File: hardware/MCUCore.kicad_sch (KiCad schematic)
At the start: 1 part, among them U1 ESP32-WROOM-32E

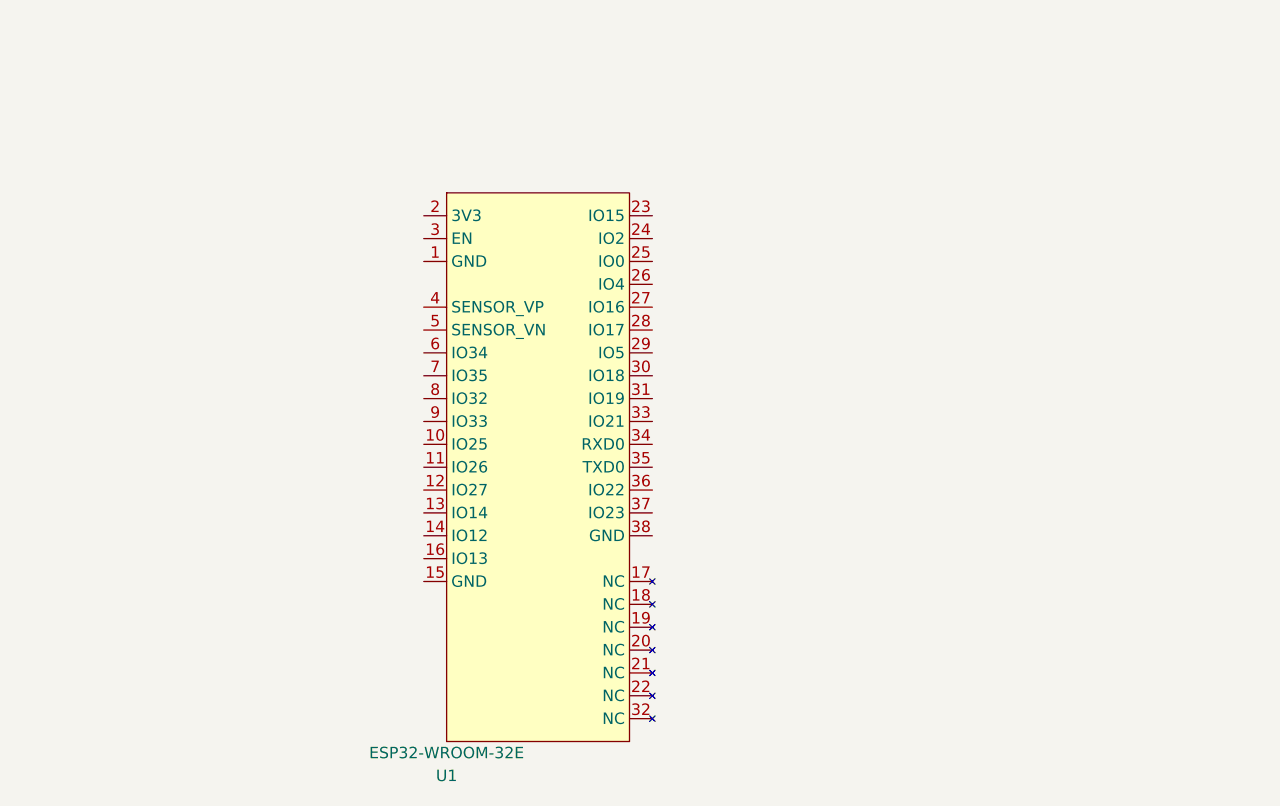
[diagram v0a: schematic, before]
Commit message: Populate MCU Core sheet
ESP32-WROOM-32E (U1) fully wired:
- Decoupling (C1 100nF + C2 1uF on 3V3/GND)
- EN: 10k pull-up + 100nF delay cap + manual RESET button
- BOOT (IO0): 10k pull-up + manual BOOT button
- nFAULT (IO15): 10k pull-up (also the MTDO safe-boot-strap default)
- UART0 header (J1, 1x4: 3V3/TX0/RX0/GND) - doubles as flashing +
  control/telemetry interface
- Expansion header (J2, 1x4: EXP1-3 on IO25/26/27 + GND) for optional
  hall/encoder sensors
- All cross-sheet signals (SPI to gate driver, SOA/SOB/SOC current
  sense, CAN TX/RX, DC-bus + temperature sense) as global labels per
  the pin map in ARCHITECTURE.md
- All 12 unused/NC pins flagged no_connect
- ERC clean except expected cross-sheet-driver warnings (will resolve
  once Power Supply/Gate Drive/Communication/Current Sensing sheets
  are wired) and a known cosmetic text-variable-resolution quirk in
  this MCP session (verified correct on disk, resolves on reopen in
  KiCad UI)

Co-Authored-By: Claude Sonnet 5 <noreply@anthropic.com>
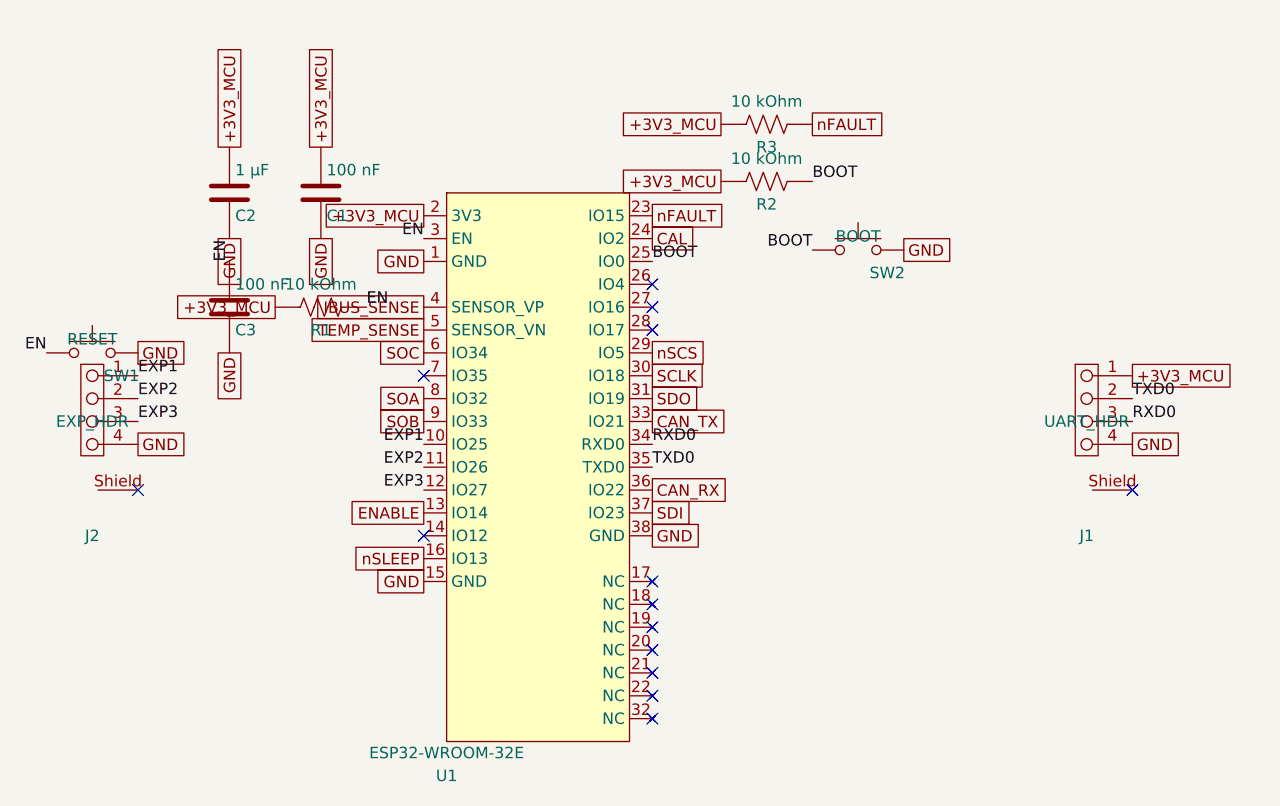
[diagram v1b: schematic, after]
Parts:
- added C1, C3: 100 nF, symbol METUPowerLab_Capacitors_Ceramics_SurfaceMounts:100 nF
- added C2: 1 µF, symbol METUPowerLab_Capacitors_Ceramics_SurfaceMounts:1 µF
- added J1: UART_HDR, METUPowerLab_Connectors_SignalConnectors:2147210040, symbol METUPowerLab_Connectors_SignalConnectors:2147210040
- added J2: EXP_HDR, METUPowerLab_Connectors_SignalConnectors:384471-E, symbol METUPowerLab_Connectors_SignalConnectors:384471-E
- added R1, R2, R3: 10 kOhm, symbol METUPowerLab_Resistors_ChipResistors:10 kOhm
- added SW1: RESET, METUPowerLab_Switches_TactileSwitches:TL6330AF200Q, symbol METUPowerLab_Switches_TactileSwitches:TL6330AF200Q
- added SW2: BOOT, METUPowerLab_Switches_TactileSwitches:TL6330AF200Q, symbol METUPowerLab_Switches_TactileSwitches:TL6330AF200Q
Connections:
- net GND: now reaches U1.1 (GND)
- net GND: now also U1.15 (GND), U1.38 (GND), C1.2, C2.2, C3.2, J1.4, J2.4, SW1.2, SW2.2
- net EXP1: now reaches U1.10 (IO25)
- net EXP1: now also J2.1
- net EXP2: now reaches U1.11 (IO26)
- net EXP2: now also J2.2
- net EXP3: now reaches U1.12 (IO27)
- net EXP3: now also J2.3
- net ENABLE: now reaches U1.13 (IO14)
- net nSLEEP: now reaches U1.16 (IO13)
- net +3V3_MCU: now reaches U1.2 (3V3)
- net +3V3_MCU: now also C1.1, C2.1, J1.1, R1.1, R2.1, R3.1
- net nFAULT: now reaches U1.23 (IO15)
- net nFAULT: now also R3.2
- net CAL: now reaches U1.24 (IO2)
- net BOOT: now reaches U1.25 (IO0)
- net BOOT: now also R2.2, SW2.1
- net nSCS: now reaches U1.29 (IO5)
- net EN: now reaches U1.3 (EN)
- net EN: now also C3.1, R1.2, SW1.1
- net SCLK: now reaches U1.30 (IO18)
- net SDO: now reaches U1.31 (IO19)
- net CAN_TX: now reaches U1.33 (IO21)
- net RXD0: now reaches U1.34 (RXD0)
- net RXD0: now also J1.3
- net TXD0: now reaches U1.35 (TXD0)
- net TXD0: now also J1.2
- net CAN_RX: now reaches U1.36 (IO22)
- net SDI: now reaches U1.37 (IO23)
- net IBUS_SENSE: now reaches U1.4 (SENSOR_VP)
- net TEMP_SENSE: now reaches U1.5 (SENSOR_VN)
- net SOC: now reaches U1.6 (IO34)
- net SOA: now reaches U1.8 (IO32)
- net SOB: now reaches U1.9 (IO33)
- no-connect marks 0 -> 14

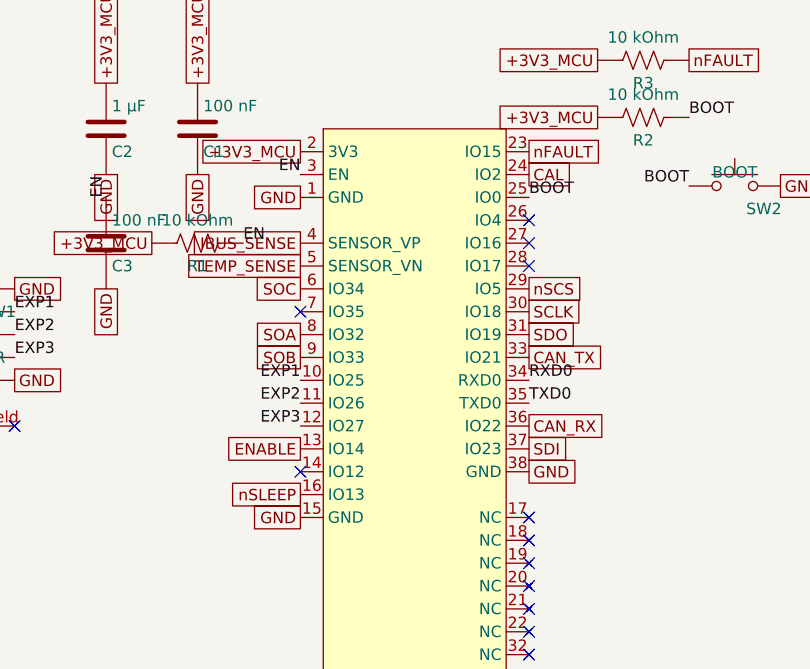
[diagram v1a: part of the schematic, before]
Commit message: Populate Gate Drive sheet (DRV8323R), fix MCU Core PWM pin gap
- DRV8323RSRGZT (=DRV8323R) fully wired per the real TI datasheet
  (SLVSDJ3D, fetched directly): single shared charge pump (not
  per-phase bootstrap caps as originally assumed), VDD/DVDD internal
  LDO decoupling only, VREF self-referenced, optional 600mA buck
  disabled (nSHD tied to GND), CAL tied to GND
- Caught and fixed a real gap before it became a wiring mistake: the
  chip needs 6 direct hardware PWM pins (INHA/INLA/INHB/INLB/INHC/
  INLC) in addition to SPI - missed in the first pass. Also removed a
  fictitious 'nSLEEP' pin that doesn't exist on this part (ENABLE
  alone controls sleep). Reassigned MCU Core GPIOs accordingly and
  added 10k pull-downs on all 6 PWM inputs + ENABLE for a safe
  power-up default (gates off until firmware takes over)
- ARCHITECTURE.md updated with corrected pin map and rationale

Co-Authored-By: Claude Sonnet 5 <noreply@anthropic.com>
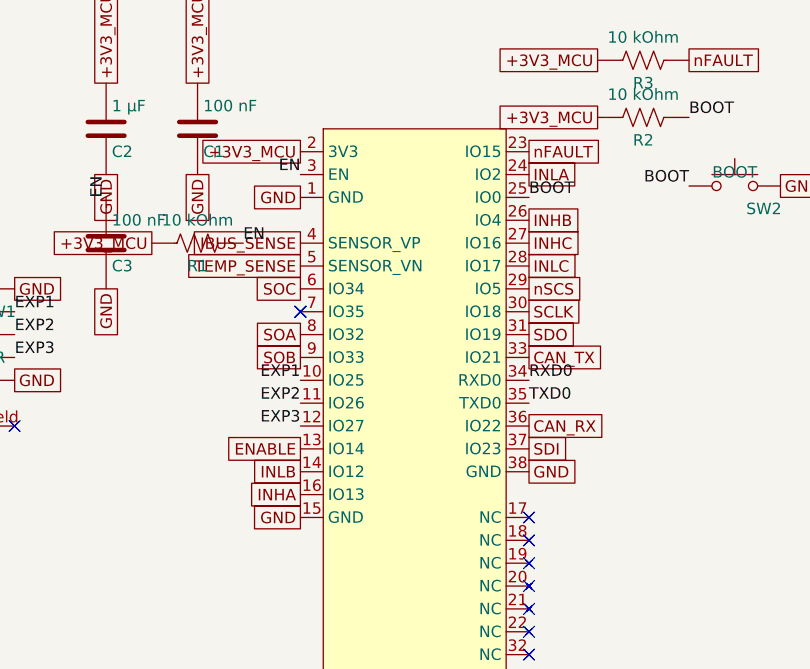
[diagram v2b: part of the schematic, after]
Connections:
- net INLB: now reaches U1.14 (IO12)
- net INHB: now reaches U1.26 (IO4)
- net INHC: now reaches U1.27 (IO16)
- net INLC: now reaches U1.28 (IO17)
- net CAL renamed INLA
- net nSLEEP renamed INHA
- no-connect marks 14 -> 11
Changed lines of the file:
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@@
-		)
-	)
-	(global_label "nSLEEP"
-		(at 116.83999999999999 110.49 180)
-		(effects
-			(font
-				(size 1.27 1.27)
-			)
-			(justify right)
 		)
 	)
@@
 		)
 	)
-	(global_label "CAL"
-		(at 142.23999999999998 74.93 0)
-		(effects
-			(font
-				(size 1.27 1.27)
-			)
-			(justify left)
-		)
-	)
 	(label "BOOT"
 		(at 142.23999999999998 77.47 0)
@@
 	)
 	(no_connect
-		(at 116.83999999999999 107.95)
-	)
-	(no_connect
 		(at 142.23999999999998 113.03)
 	)
@@
 	(no_connect
 		(at 142.23999999999998 125.72999999999999)
-	)
-	(no_connect
-		(at 142.23999999999998 80.00999999999999)
-	)
-	(no_connect
-		(at 142.23999999999998 82.55)
-	)
-	(no_connect
-		(at 142.23999999999998 85.09)
 	)
 	(no_connect
@@
 		(effects
 			(font
+				(size 1.27 1.27)
+			)
+			(justify left)
+		)
+	)
+	(no_connect
+		(at 116.83999999999999 90.17)
+	)
+	(global_label "INHA"
+		(at 116.83999999999999 110.49 180)
+		(effects
+			(font
+				(size 1.27 1.27)
+			)
+			(justify right)
+		)
+	)
+	(global_label "INLB"
+		(at 116.83999999999999 107.95 180)
+		(effects
+			(font
+				(size 1.27 1.27)
+			)
+			(justify right)
+		)
+	)
+	(global_label "INLA"
+		(at 142.23999999999998 74.93 0)
+		(effects
+			(font
+				(size 1.27 1.27)
+			)
+			(justify left)
+		)
+	)
+	(global_label "INHC"
+		(at 142.23999999999998 82.55 0)
+		(effects
+			(font
+				(size 1.27 1.27)
+			)
+			(justify left)
+		)
+	)
+	(global_label "INLC"
+		(at 142.23999999999998 85.09 0)
+		(effects
+			(font
+				(size 1.27 1.27)
+			)
+			(justify left)
+		)
+	)
+	(global_label "INHB"
+		(at 142.23999999999998 80.00999999999999 0)
+		(effects
+			(font

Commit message: PCB layout: board outline, mounting holes, footprint placement, copper pours, phase-output routing
- 100x115mm 2-layer board, 4x M3 mounting holes, design rules per PowerLab spec
- All 55 schematic components synced to board with real footprints
- Auto-placed via force-directed placement with locked connector/MCU anchors
- GND pour (both layers) + localized pours for VIN_RAW/+VBUS/+VBUS_EFUSE_OUT/+VBUS_PROT/+5V_LOGIC
- Routed the 3 critical phase-output traces (SHA/SHB/SHC, 2mm wide)
- Documented full PCB status in ARCHITECTURE.md: NOT yet fab-ready (732 DRC
  violations, 21 courtyard overlaps, ~50 signal nets still unrouted since
  Freerouting is unavailable in this environment)

Co-Authored-By: Claude Sonnet 5 <noreply@anthropic.com>
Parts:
- C1, C2, C3: footprint (none) -> METUPowerLab_Capacitors_Ceramics_SurfaceMounts:0603_Medium
- R1, R2, R3: footprint (none) -> METUPowerLab_Resistors_ChipResistors:0603_Medium
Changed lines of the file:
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@@
 			)
 		)
-		(property "Footprint" ""
+		(property "Footprint" "METUPowerLab_Capacitors_Ceramics_SurfaceMounts:0603_Medium"
 			(at 106.375 66.04 0)
 			(hide yes)
@@
 			)
 		)
-		(property "Footprint" ""
+		(property "Footprint" "METUPowerLab_Capacitors_Ceramics_SurfaceMounts:0603_Medium"
 			(at 96.215 66.04 0)
 			(hide yes)
@@
 			)
 		)
-		(property "Footprint" ""
+		(property "Footprint" "METUPowerLab_Resistors_ChipResistors:0603_Medium"
 			(at 106.426 82.296 90)
 			(hide yes)
@@
 			)
 		)
-		(property "Footprint" ""
+		(property "Footprint" "METUPowerLab_Capacitors_Ceramics_SurfaceMounts:0603_Medium"
 			(at 96.215 78.74 0)
 			(hide yes)
@@
 			)
 		)
-		(property "Footprint" ""
+		(property "Footprint" "METUPowerLab_Resistors_ChipResistors:0603_Medium"
 			(at 155.956 68.326 90)
 			(hide yes)
@@
 			)
 		)
-		(property "Footprint" ""
+		(property "Footprint" "METUPowerLab_Resistors_ChipResistors:0603_Medium"
 			(at 155.956 61.976 90)
 			(hide yes)
